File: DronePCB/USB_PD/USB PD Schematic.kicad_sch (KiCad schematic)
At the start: 22 parts, among them J1 USB_C_Receptacle_PowerOnly_6P, U3 CYPD3177-24LQXQT, U4 DMP3098LSD-13, U5 DMP3098LSD-13

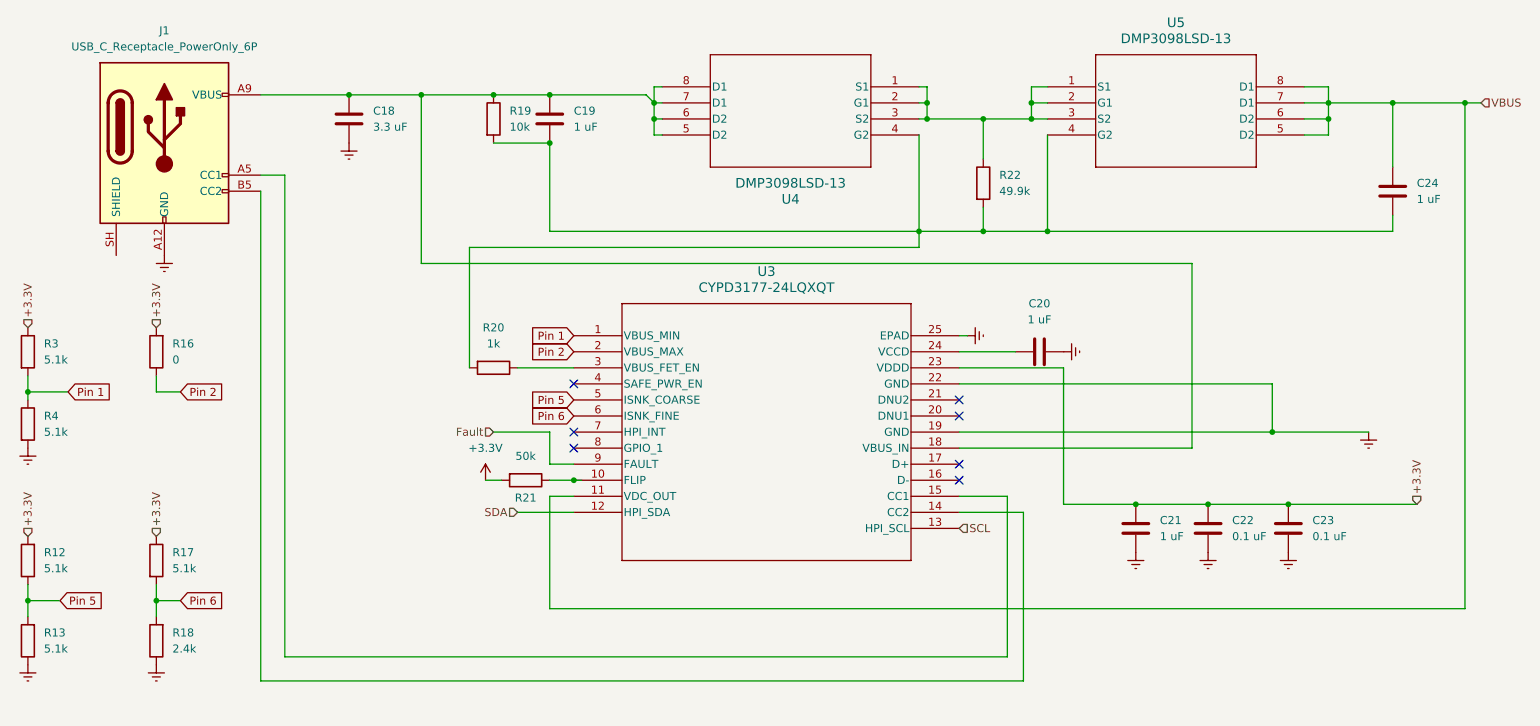
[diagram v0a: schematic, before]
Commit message: Completed H-Bridge Circuit | Finished Schematic | Working on pcb design
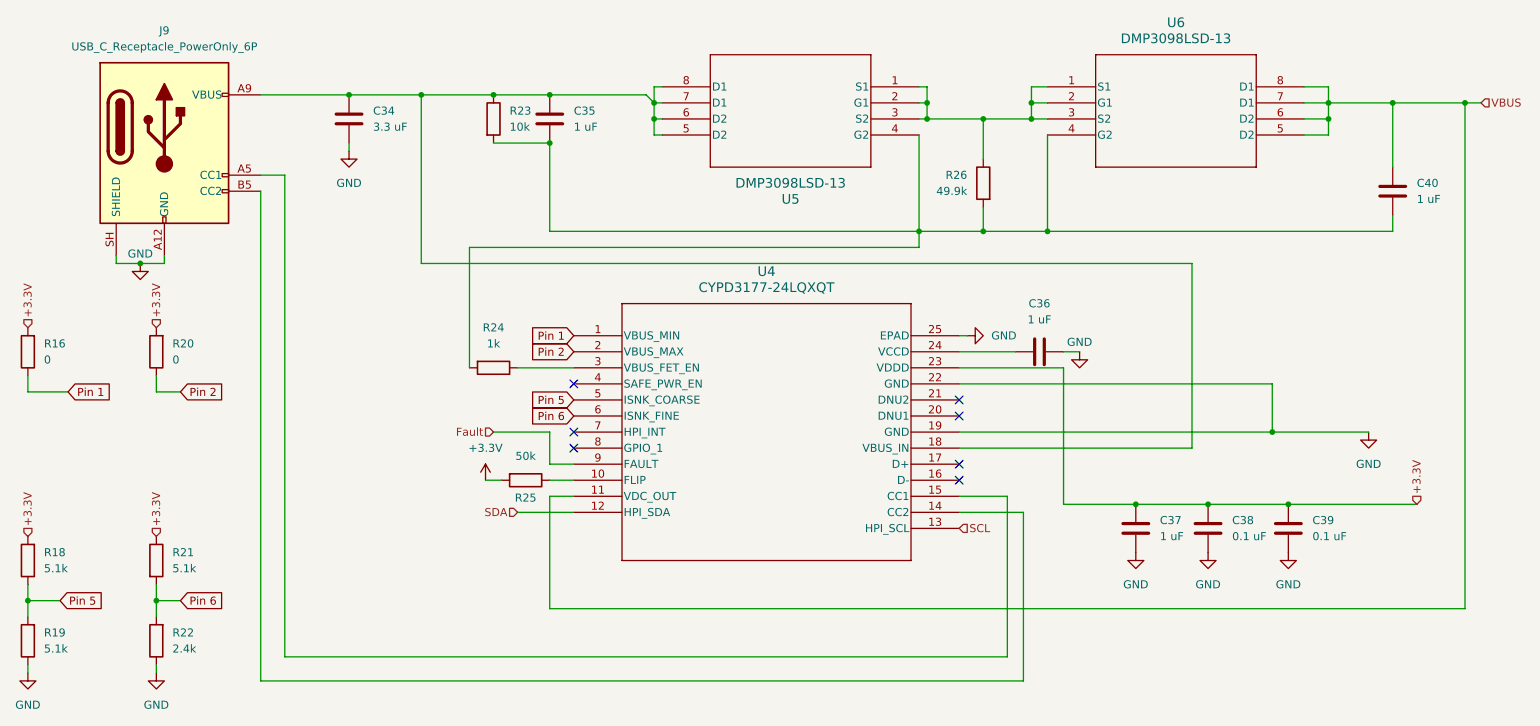
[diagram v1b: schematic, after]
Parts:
- removed R3, R4: 5.1k, symbol Device:R
- added R16: 0, Resistor_SMD:R_0603_1608Metric, symbol Device:R
- C34: renamed from C18; footprint (none) -> Capacitor_SMD:C_0603_1608Metric
- C35: renamed from C19; footprint (none) -> Capacitor_SMD:C_0603_1608Metric
- C36: renamed from C20; footprint (none) -> Capacitor_SMD:C_0603_1608Metric
- C37: renamed from C21; footprint (none) -> Capacitor_SMD:C_0603_1608Metric
- C38: renamed from C22; footprint (none) -> Capacitor_SMD:C_0603_1608Metric
- C39: renamed from C23; footprint (none) -> Capacitor_SMD:C_0603_1608Metric
- C40: renamed from C24; footprint (none) -> Capacitor_SMD:C_0603_1608Metric
- J9: renamed from J1; footprint (none) -> Connector_USB:USB_C_Receptacle_GCT_USB4125-xx-x_6P_TopMnt_Horizontal
- R18: renamed from R12; footprint (none) -> Resistor_SMD:R_0603_1608Metric
- R19: renamed from R13; footprint (none) -> Resistor_SMD:R_0603_1608Metric
- R20: renamed from R16; footprint (none) -> Resistor_SMD:R_0603_1608Metric
- R21: renamed from R17; footprint (none) -> Resistor_SMD:R_0603_1608Metric
- R22: renamed from R18; footprint (none) -> Resistor_SMD:R_0603_1608Metric
- R23: renamed from R19; footprint (none) -> Resistor_SMD:R_0603_1608Metric
- R24: renamed from R20; footprint (none) -> Resistor_SMD:R_0603_1608Metric
- R25: renamed from R21; footprint (none) -> Resistor_SMD:R_0603_1608Metric
- R26: renamed from R22; footprint (none) -> Resistor_SMD:R_0603_1608Metric
- U4: renamed from U3; footprint QFN24_CYPD3177-24LQXQT_INF -> ExternalParts:QFN24_CYPD3177-24LQXQT_INF
- U5: renamed from U4; footprint SOP_DMP3098LSD-13_DIO -> ExternalParts:SOP_DMP3098LSD-13_DIO
- U6: renamed from U5; footprint SOP_DMP3098LSD-13_DIO -> ExternalParts:SOP_DMP3098LSD-13_DIO
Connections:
- net Earth is gone; now on net GND: C34.2, C36.1, C37.2, C38.2, C39.2, J9.A12 (GND), J9.B12 (GND), R19.1, R22.1, U4.19 (GND), U4.22 (GND), U4.25 (EPAD)
- net +3.3V: now also R16.2
- net Pin 1: now also R16.1
- net GND: now reaches J9.SH (SHIELD)

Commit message: All circuits complete
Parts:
- renumbered J9 to J8, R16 to R18, R18 to R19, R19 to R20, R20 to R21, R21 to R22, R22 to R23, R23 to R24, R24 to R25, R25 to R26, R26 to R27
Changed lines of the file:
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@@
 		(dnp no)
 		(fields_autoplaced yes)
-		(property "Reference" "#PWR044"
+		(property "Reference" "#PWR046"
 			(at 43.18 140.97 0)
 			(hide yes)
@@
 			(project "DronePCB"
 				(path "/c9b74494-ac48-4f27-9459-39f0e04d9d05/59dcabd2-13f8-43f8-9fec-3f0511ac7fcb"
-					(reference "#PWR044")
+					(reference "#PWR046")
 					(unit 1)
 				)
@@
 		(dnp no)
 		(fields_autoplaced yes)
-		(property "Reference" "#PWR042"
+		(property "Reference" "#PWR047"
 			(at 73.66 58.42 0)
 			(hide yes)
@@
 			(project "DronePCB"
 				(path "/c9b74494-ac48-4f27-9459-39f0e04d9d05/59dcabd2-13f8-43f8-9fec-3f0511ac7fcb"
-					(reference "#PWR042")
+					(reference "#PWR047")
 					(unit 1)
 				)
@@
 		(dnp no)
 		(fields_autoplaced yes)
-		(property "Reference" "#PWR046"
+		(property "Reference" "#PWR051"
 			(at 198.12 121.92 0)
 			(hide yes)
@@
 			(project "DronePCB"
 				(path "/c9b74494-ac48-4f27-9459-39f0e04d9d05/59dcabd2-13f8-43f8-9fec-3f0511ac7fcb"
-					(reference "#PWR046")
+					(reference "#PWR051")
 					(unit 1)
 				)
@@
 		(dnp no)
 		(fields_autoplaced yes)
-		(property "Reference" "R20"
+		(property "Reference" "R21"
 			(at 45.72 82.5499 0)
 			(show_name no)
@@
 			(project "DronePCB"
 				(path "/c9b74494-ac48-4f27-9459-39f0e04d9d05/59dcabd2-13f8-43f8-9fec-3f0511ac7fcb"
-					(reference "R20")
+					(reference "R21")
 					(unit 1)
 				)
@@
 		(dnp no)
 		(fields_autoplaced yes)
-		(property "Reference" "#PWR050"
+		(property "Reference" "#PWR053"
 			(at 222.25 121.92 0)
 			(hide yes)
@@
 			(project "DronePCB"
 				(path "/c9b74494-ac48-4f27-9459-39f0e04d9d05/59dcabd2-13f8-43f8-9fec-3f0511ac7fcb"
-					(reference "#PWR050")
+					(reference "#PWR053")
 					(unit 1)
 				)
@@
 		(dnp no)
 		(fields_autoplaced yes)
-		(property "Reference" "#PWR051"
+		(property "Reference" "#PWR054"
 			(at 234.95 102.87 0)
 			(hide yes)
@@
 			(project "DronePCB"
 				(path "/c9b74494-ac48-4f27-9459-39f0e04d9d05/59dcabd2-13f8-43f8-9fec-3f0511ac7fcb"
-					(reference "#PWR051")
+					(reference "#PWR054")
 					(unit 1)
 				)
@@
 		(dnp no)
 		(fields_autoplaced yes)
-		(property "Reference" "R21"
+		(property "Reference" "R22"
 			(at 45.72 115.5699 0)
 			(show_name no)
@@
 			(project "DronePCB"
 				(path "/c9b74494-ac48-4f27-9459-39f0e04d9d05/59dcabd2-13f8-43f8-9fec-3f0511ac7fcb"
-					(reference "R21")
+					(reference "R22")
 					(unit 1)
 				)
@@
 		(in_pos_files yes)
 		(dnp no)
-		(property "Reference" "R25"
+		(property "Reference" "R26"
 			(at 101.6 106.934 90)
 			(show_name no)
@@
 			(project "DronePCB"
 				(path "/c9b74494-ac48-4f27-9459-39f0e04d9d05/59dcabd2-13f8-43f8-9fec-3f0511ac7fcb"
-					(reference "R25")
+					(reference "R26")
 					(unit 1)
 				)
@@
 		(in_pos_files yes)
 		(dnp no)
-		(property "Reference" "R23"
+		(property "Reference" "R24"
 			(at 99.06 45.72 0)
 			(show_name no)
@@
 			(project "DronePCB"
 				(path "/c9b74494-ac48-4f27-9459-39f0e04d9d05/59dcabd2-13f8-43f8-9fec-3f0511ac7fcb"
-					(reference "R23")
+					(reference "R24")
 					(unit 1)
 				)
@@
 		(dnp no)
 		(fields_autoplaced yes)
-		(property "Reference" "#PWR047"
+		(property "Reference" "#PWR048"
 			(at 95.25 107.95 0)
 			(hide yes)
@@
 			(project "DronePCB"
 				(path "/c9b74494-ac48-4f27-9459-39f0e04d9d05/59dcabd2-13f8-43f8-9fec-3f0511ac7fcb"
-					(reference "#PWR047")
+					(reference "#PWR048")
 					(unit 1)
 				)
@@
 		(dnp no)
 		(fields_autoplaced yes)
-		(property "Reference" "#PWR052"
+		(property "Reference" "#PWR049"
 			(at 177.8 81.28 0)
 			(hide yes)
@@
 			(project "DronePCB"
 				(path "/c9b74494-ac48-4f27-9459-39f0e04d9d05/59dcabd2-13f8-43f8-9fec-3f0511ac7fcb"
-					(reference "#PWR052")
+					(reference "#PWR049")
 					(unit 1)
 				)
@@
 		(dnp no)
 		(fields_autoplaced yes)
-		(property "Reference" "R16"
+		(property "Reference" "R18"
 			(at 25.4 82.5499 0)
 			(show_name no)
@@
 			(project "DronePCB"
 				(path "/c9b74494-ac48-4f27-9459-39f0e04d9d05/59dcabd2-13f8-43f8-9fec-3f0511ac7fcb"
-					(reference "R16")
+					(reference "R18")
 					(unit 1)
 				)
@@
 		(dnp no)
 		(fields_autoplaced yes)
-		(property "Reference" "#PWR043"
+		(property "Reference" "#PWR044"
 			(at 22.86 140.97 0)
 			(hide yes)
@@
 			(project "DronePCB"
 				(path "/c9b74494-ac48-4f27-9459-39f0e04d9d05/59dcabd2-13f8-43f8-9fec-3f0511ac7fcb"
-					(reference "#PWR043")
+					(reference "#PWR044")
 					(unit 1)
 				)
@@
 		(dnp no)
 		(fields_autoplaced yes)
-		(property "Reference" "R18"
+		(property "Reference" "R19"
 			(at 25.4 115.5699 0)
 			(show_name no)
@@
 			(project "DronePCB"
 				(path "/c9b74494-ac48-4f27-9459-39f0e04d9d05/59dcabd2-13f8-43f8-9fec-3f0511ac7fcb"
-					(reference "R18")
+					(reference "R19")
 					(unit 1)
 				)
@@
 		(dnp no)
 		(fields_autoplaced yes)
-		(property "Reference" "R24"
+		(property "Reference" "R25"
 			(at 96.52 80.01 90)
 			(show_name no)
@@
 			(project "DronePCB"
 				(path "/c9b74494-ac48-4f27-9459-39f0e04d9d05/59dcabd2-13f8-43f8-9fec-3f0511ac7fcb"
-					(reference "R24")
+					(reference "R25")
 					(unit 1)
 				)
@@
 		(in_pos_files yes)
 		(dnp no)
-		(property "Reference" "#PWR053"
+		(property "Reference" "#PWR050"
 			(at 189.23 90.17 0)
 			(hide yes)
@@
 			(project "DronePCB"
 				(path "/c9b74494-ac48-4f27-9459-39f0e04d9d05/59dcabd2-13f8-43f8-9fec-3f0511ac7fcb"
-					(reference "#PWR053")
+					(reference "#PWR050")
 					(unit 1)
 				)
@@
 		(in_pos_files yes)
 		(dnp no)
-		(property "Reference" "R26"
+		(property "Reference" "R27"
 			(at 171.45 55.8799 0)
 			(show_name no)
@@
 			(project "DronePCB"
 				(path "/c9b74494-ac48-4f27-9459-39f0e04d9d05/59dcabd2-13f8-43f8-9fec-3f0511ac7fcb"
-					(reference "R26")
+					(reference "R27")
 					(unit 1)
 				)
@@
 		(dnp no)
 		(fields_autoplaced yes)
-		(property "Reference" "J9"
+		(property "Reference" "J8"
 			(at 44.45 33.02 0)
 			(show_name no)
@@
 			(project "DronePCB"
 				(path "/c9b74494-ac48-4f27-9459-39f0e04d9d05/59dcabd2-13f8-43f8-9fec-3f0511ac7fcb"
-					(reference "J9")
+					(reference "J8")
 					(unit 1)
 				)
@@
 		(dnp no)
 		(fields_autoplaced yes)
-		(property "Reference" "R22"
+		(property "Reference" "R23"
 			(at 45.72 128.2699 0)
 			(show_name no)
@@
 			(project "DronePCB"
 				(path "/c9b74494-ac48-4f27-9459-39f0e04d9d05/59dcabd2-13f8-43f8-9fec-3f0511ac7fcb"
-					(reference "R22")
+					(reference "R23")
 					(unit 1)
 				)
@@
 		(dnp no)
 		(fields_autoplaced yes)
-		(property "Reference" "#PWR049"
+		(property "Reference" "#PWR052"
 			(at 209.55 121.92 0)
 			(hide yes)
@@
 			(project "DronePCB"
 				(path "/c9b74494-ac48-4f27-9459-39f0e04d9d05/59dcabd2-13f8-43f8-9fec-3f0511ac7fcb"
-					(reference "#PWR049")
+					(reference "#PWR052")
 					(unit 1)
 				)
@@
 		(dnp no)
 		(fields_autoplaced yes)
-		(property "Reference" "R19"
+		(property "Reference" "R20"
 			(at 25.4 128.2699 0)
 			(show_name no)
@@
 			(project "DronePCB"
 				(path "/c9b74494-ac48-4f27-9459-39f0e04d9d05/59dcabd2-13f8-43f8-9fec-3f0511ac7fcb"
-					(reference "R19")
-					(unit 1)
-				)
+					(reference "R20")
+					(unit 1)
+				)
